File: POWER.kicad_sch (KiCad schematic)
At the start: 53 parts, among them J1 Conn_01x03, SW1 TS-1010-C-A, U1 RT5750A, U2 RT9467, U3 RT4812, U5 RT6150, U6 RT5750A, U7 RT5750A

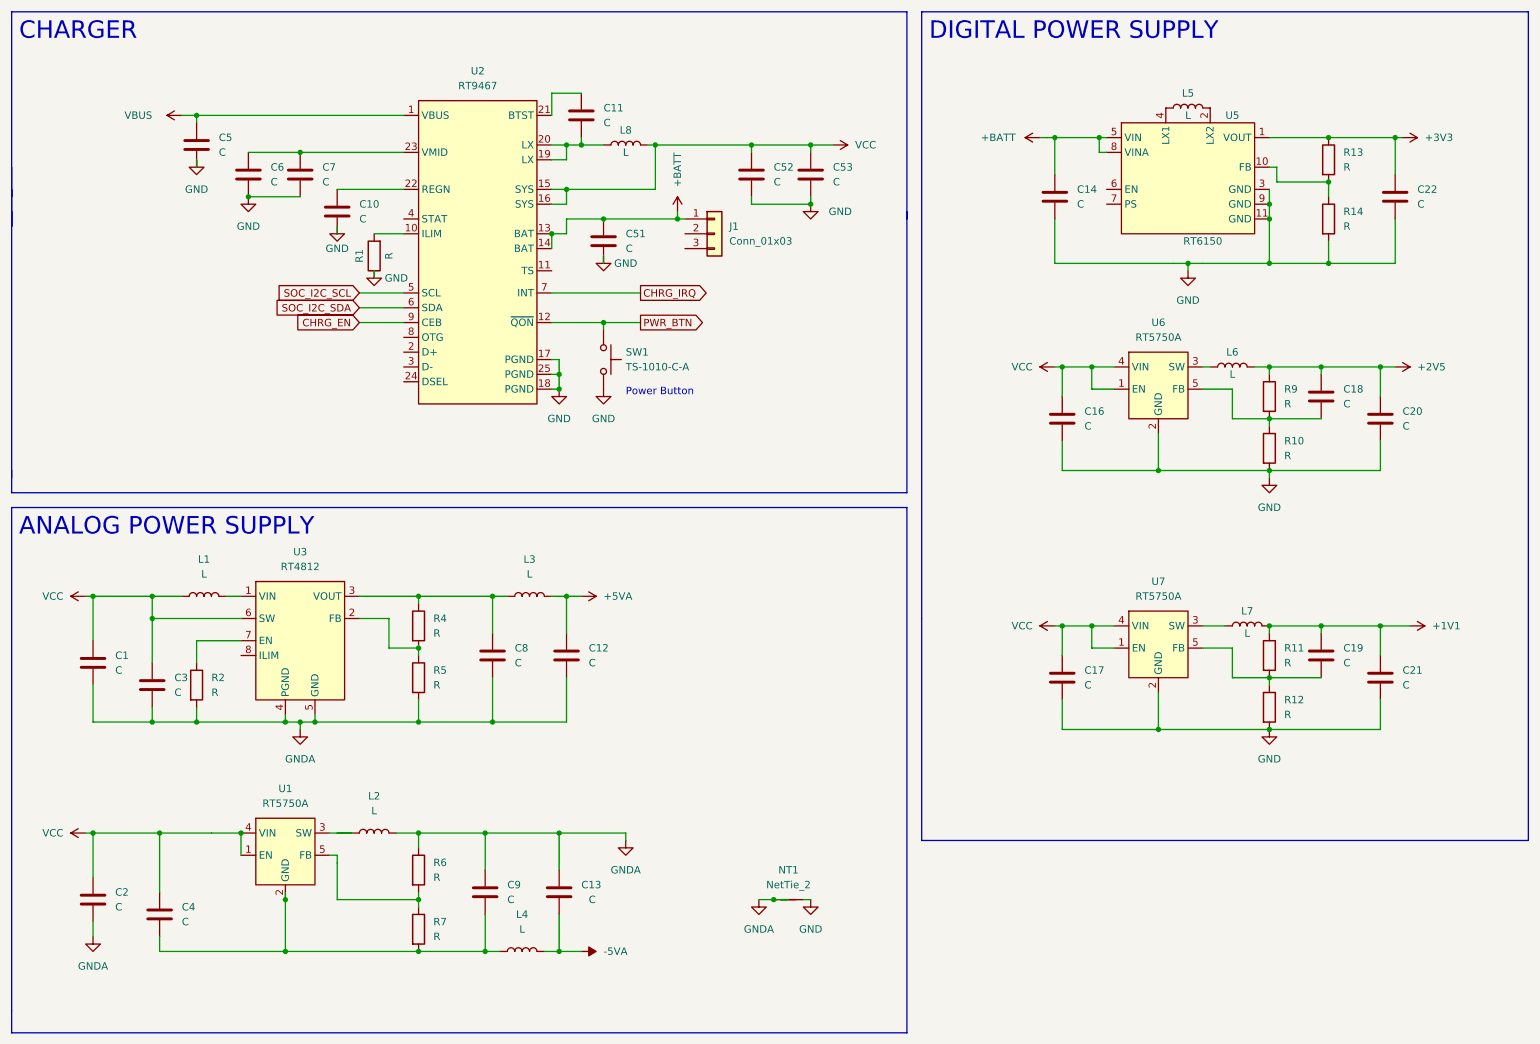
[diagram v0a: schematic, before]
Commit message: adde power source 3v0, molex connector, restistor footprints
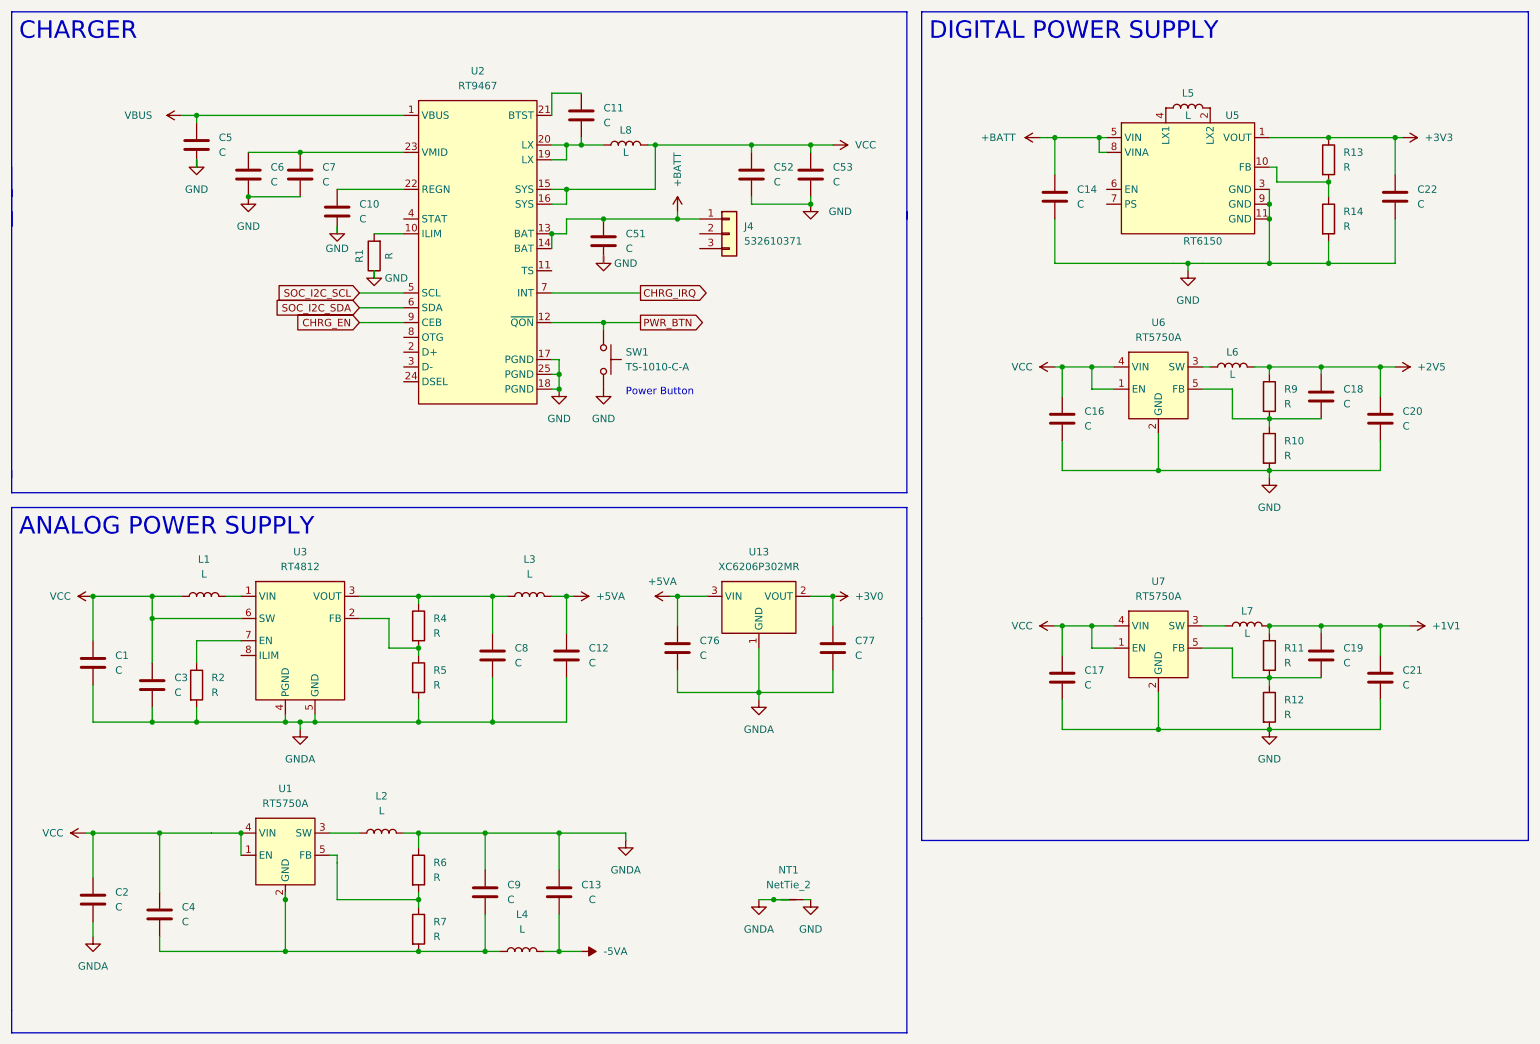
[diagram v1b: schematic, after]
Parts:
- removed J1: Conn_01x03, symbol Connector_Generic:Conn_01x03
- added C76, C77: C, symbol rlib_passive:C
- added J4: 532610371, rlib_connectors:MOLEX_532610371, symbol rlib_connectors:532610371
- added U13: XC6206P302MR, rlib_power:SOT-23, symbol rlib_power:XC6206P302MR
- R1, R10, R11, R12, R13, R14, R2, R4, R5, R6, R7, R9: footprint (none) -> rlib_passive:R_0603_1608Metric
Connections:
- net +5VA: now also C76.1, U13.3 (VIN)
- net +BATT: now also J4.1 (Pin_1)
- net GNDA: now also C76.2, C77.2, U13.1 (GND)
- new net +3V0: C77.1, U13.2 (VOUT)
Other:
- moved on the sheet: L2

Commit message: added winstar display
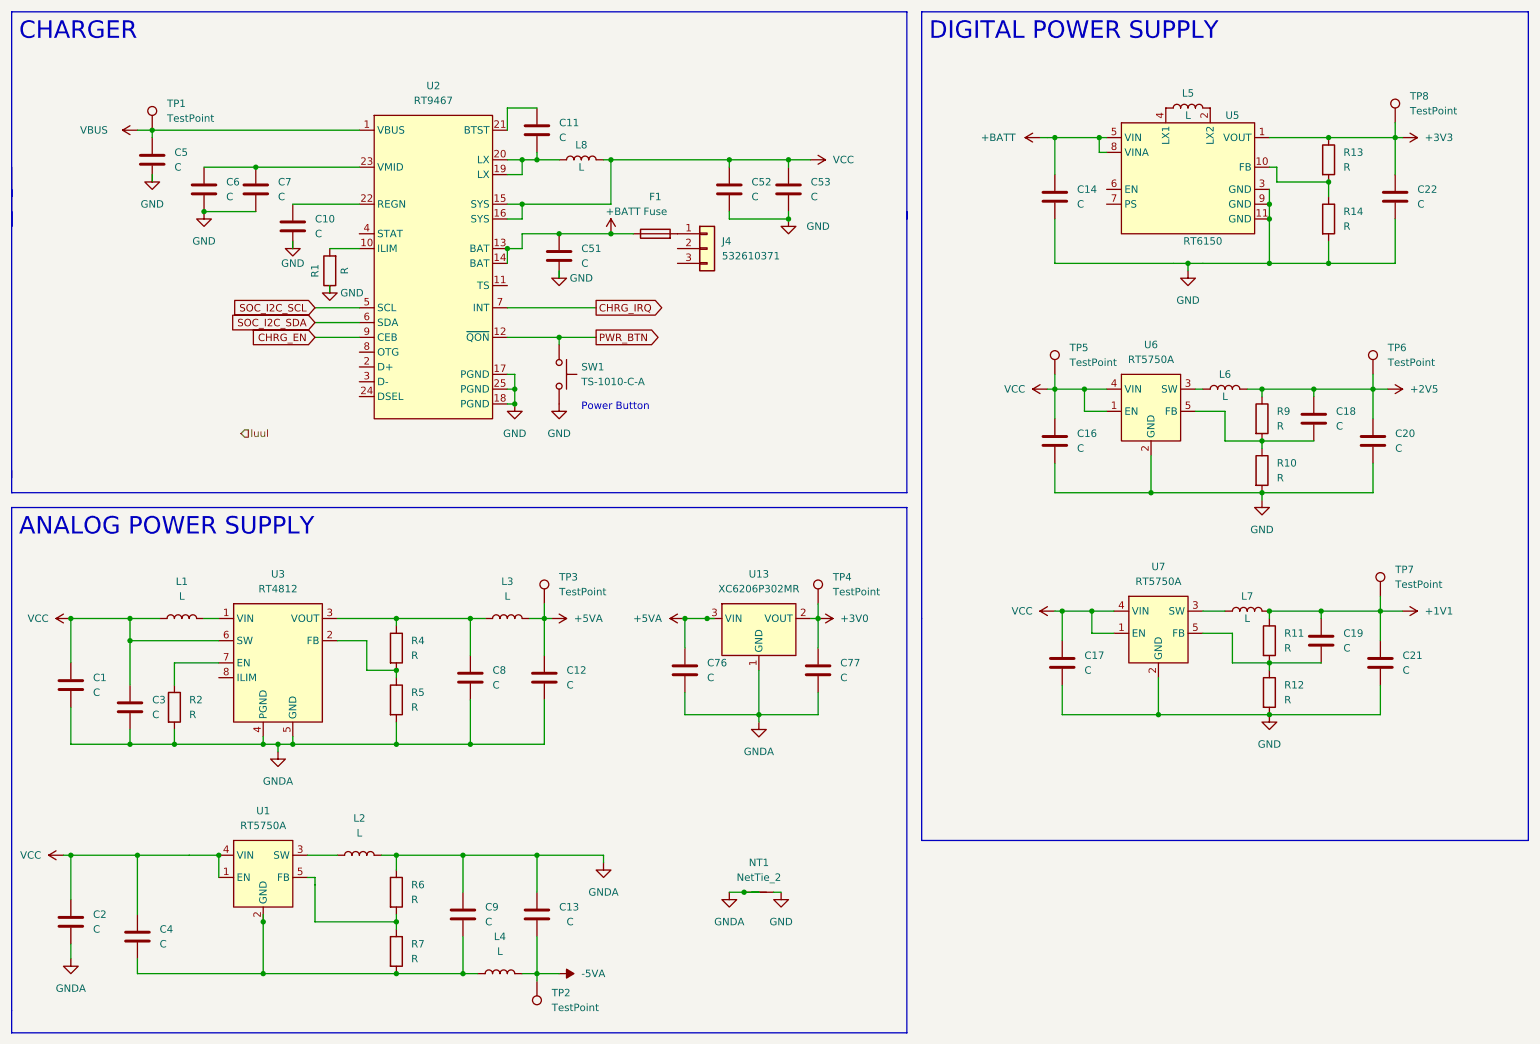
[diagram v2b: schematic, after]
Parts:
- added F1: Fuse, symbol Device:Fuse
- added TP1, TP2, TP3, TP4, TP5, TP6, TP7, TP8: TestPoint, symbol Connector:TestPoint
- C1, C10, C11, C12, C13, C14, C16, C17, C18, C19, C2, C20, C21, C22, C3, C4, C5, C51, C52, C53, C6, C7, C76, C77, C8, C9: footprint (none) -> rlib_passive:C_0603_1608Metric
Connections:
- net +1V1: now also TP7.1
- net +2V5: now also TP6.1
- net +3V0: now also TP4.1
- net +3V3: now also TP8.1
- net +5VA: now also TP3.1
- net +BATT: now also F1.1; no longer J4.1 (Pin_1)
- net -5VA: now also TP2.1
- net VBUS: now also TP1.1
- net VCC: now also TP5.1
- new net: F1.2, J4.1 (Pin_1)
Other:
- moved on the sheet: C1, C10, C11, C12, C13, C16, C17, C18, C19, C2, C20, C21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
